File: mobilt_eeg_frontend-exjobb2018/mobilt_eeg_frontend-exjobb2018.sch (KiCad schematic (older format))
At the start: 116 parts, among them J1 Conn_02x04_Odd_Even, J11 Conn_01x02, J2 Conn_02x20_Odd_Even, J3 Conn_02x04_Odd_Even, J5 Data Header, J8 Conn_01x08, J9 Conn_01x04, P1 Conn_02x20_Odd_Even, SW1 SW_DIP_x01, SW2 SW_DIP_x01, U1 ADS1299-4PAG, U2 TPS60403DBVR, U3 TPS72325DBVT, U4 TPS73225DBVT, U5 TPS73233DBVT, U6 CAT24C256, X1 X1G0044810050_SG7050CAN_2.048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

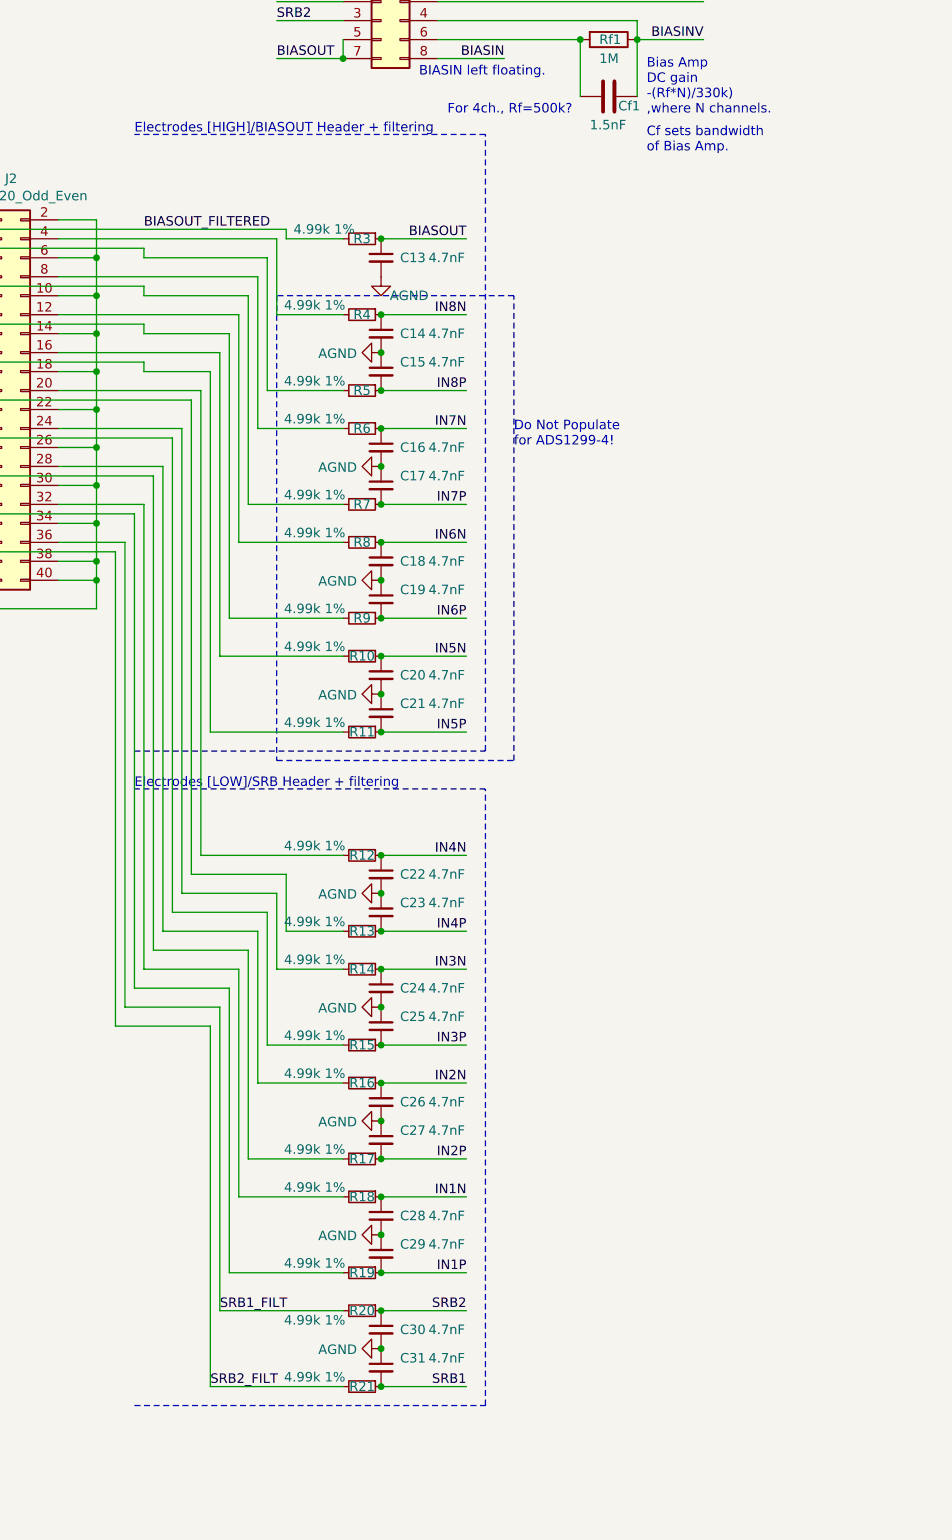
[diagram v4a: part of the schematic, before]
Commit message: added differential capacitors on each channel with DNP value.
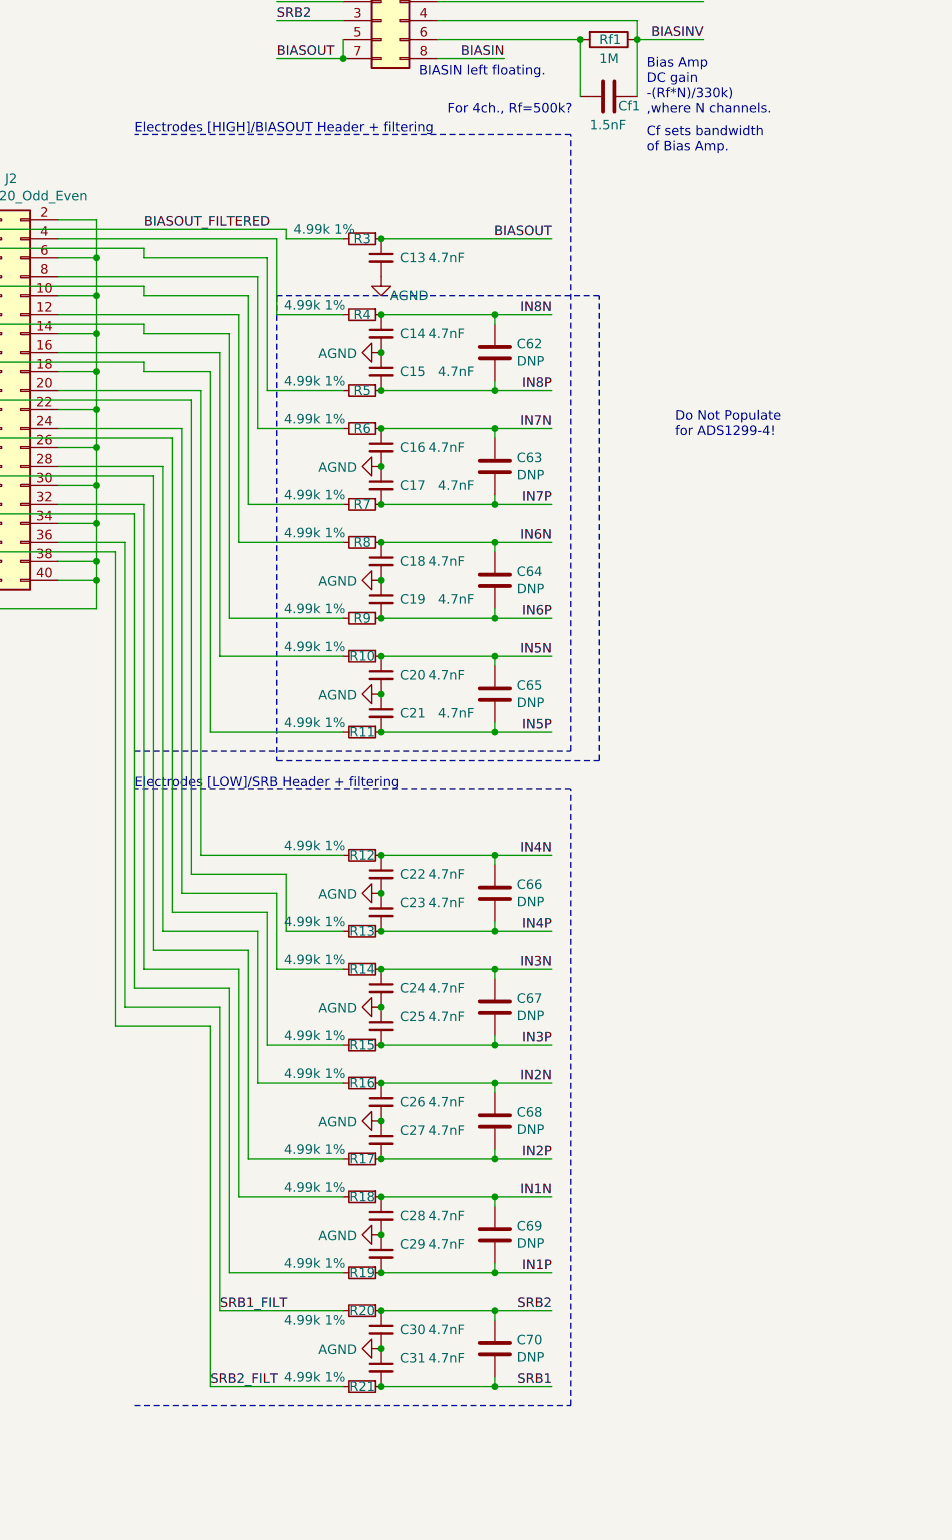
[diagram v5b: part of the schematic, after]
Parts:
- added C62, C63, C64, C65, C66, C67, C68, C69, C70: DNP, Capacitors_SMD:C_0805_HandSoldering, symbol Device:C
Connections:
- wire segments 498 -> 534

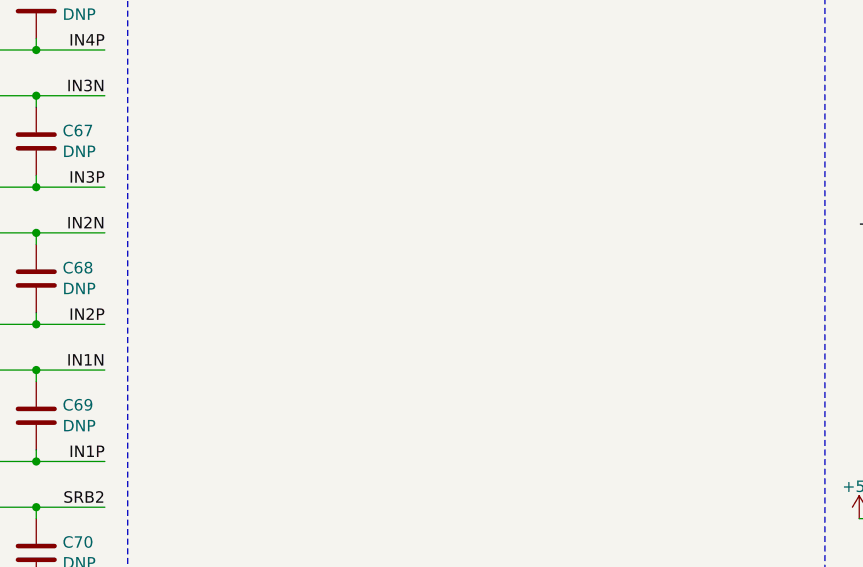
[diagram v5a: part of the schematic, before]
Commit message: Changed footprints for resistors and caps to one that encloses the pads.
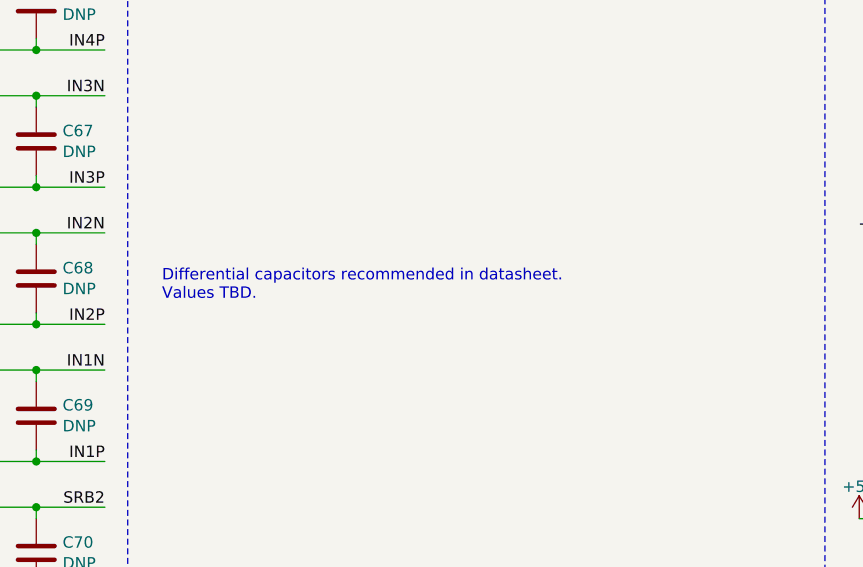
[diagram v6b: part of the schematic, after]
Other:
- note added: "Differential capacitors recommended in datasheet.\nValues TBD."
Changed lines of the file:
@@
 Wire Wire Line
 	3600 9700 3900 9700
+Text Notes 4150 8400 0    50   ~ 0
+Differential capacitors recommended in datasheet.\nValues TBD.
 $EndSCHEMATC

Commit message: connected hanging AVDD
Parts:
- MK1, MK2, MK3, MK4: symbol Mechanical:Mounting_Hole -> mobilt_eeg_frontend-exjobb2018-rescue:Mounting_Hole-Mechanical
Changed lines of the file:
@@
 ID_SD and ID_SC PINS:\nThese pins are reserved for HAT ID EEPROM.\n\nAt boot time this I2C interface will be\ninterrogated to look for an EEPROM\nthat identifes the attached board and\nallows automagic setup of the GPIOs\n(and optionally, Linux drivers).\n\nDO NOT USE these pins for anything other\nthan attaching an I2C ID EEPROM. Leave\nunconnected if ID EEPROM not required.
 $Comp
-L Mechanical:Mounting_Hole MK1
+L mobilt_eeg_frontend-exjobb2018-rescue:Mounting_Hole-Mechanical MK1
 U 1 1 5834FB2E
 P -900 2250
@@
 $EndComp
 $Comp
-L Mechanical:Mounting_Hole MK3
+L mobilt_eeg_frontend-exjobb2018-rescue:Mounting_Hole-Mechanical MK3
 U 1 1 5834FBEF
 P -450 2250
@@
 $EndComp
 $Comp
-L Mechanical:Mounting_Hole MK2
+L mobilt_eeg_frontend-exjobb2018-rescue:Mounting_Hole-Mechanical MK2
 U 1 1 5834FC19
 P -900 2450
@@
 $EndComp
 $Comp
-L Mechanical:Mounting_Hole MK4
+L mobilt_eeg_frontend-exjobb2018-rescue:Mounting_Hole-Mechanical MK4
 U 1 1 5834FC4F
 P -450 2450
